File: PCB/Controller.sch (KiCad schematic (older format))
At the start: 1 part

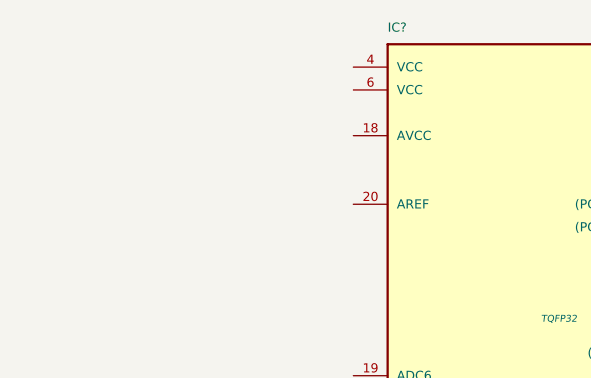
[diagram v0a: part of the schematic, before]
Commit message: Started the schematic. Added the power circuit
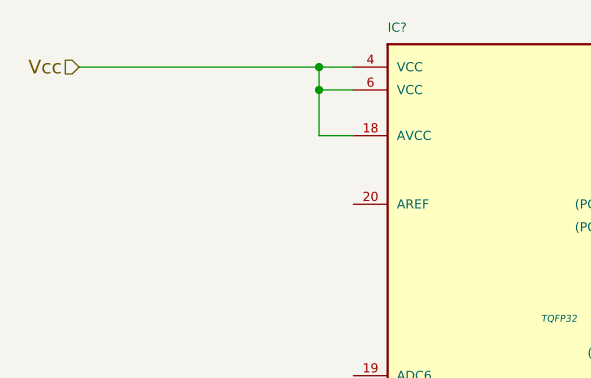
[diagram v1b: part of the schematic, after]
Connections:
- net Vcc: now reaches IC?.18 (AVCC)
- net Vcc: now also IC?.4 (VCC), IC?.6 (VCC)
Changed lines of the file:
@@
 LIBS:memory
 LIBS:xilinx
-LIBS:special
 LIBS:microcontrollers
 LIBS:dsp
@@
 LIBS:contrib
 LIBS:valves
+LIBS:Tfac-Symbols
+LIBS:TfaC-cache
 EELAYER 25 0
 EELAYER END
@@
 	3750 4500 3450 4500
 Connection ~ 3450 4500
+Text HLabel 2550 2200 0    60   Input ~ 0
+Vcc
+Wire Wire Line
+	2550 2200 3750 2200
+Wire Wire Line
+	3600 2200 3600 2500
+Wire Wire Line
+	3600 2300 3750 2300
+Connection ~ 3600 2200
+Wire Wire Line
+	3600 2500 3750 2500
+Connection ~ 3600 2300
 $EndSCHEMATC

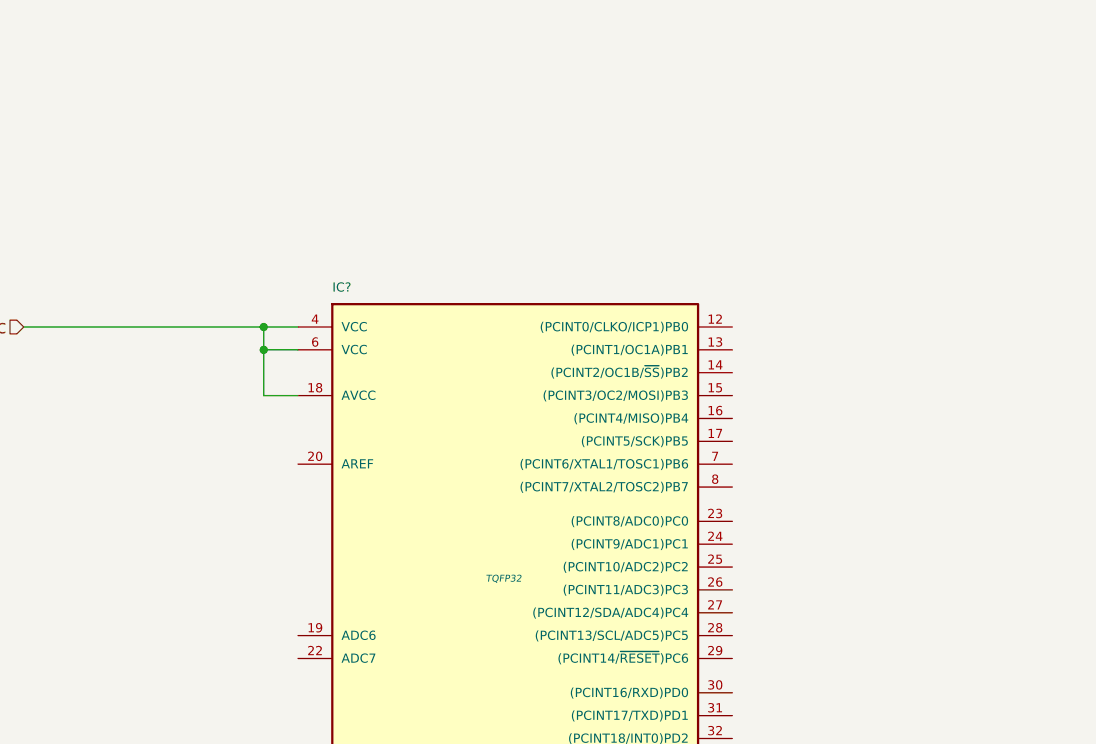
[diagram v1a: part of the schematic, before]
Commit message: Updated the schematic for the RTC and controller
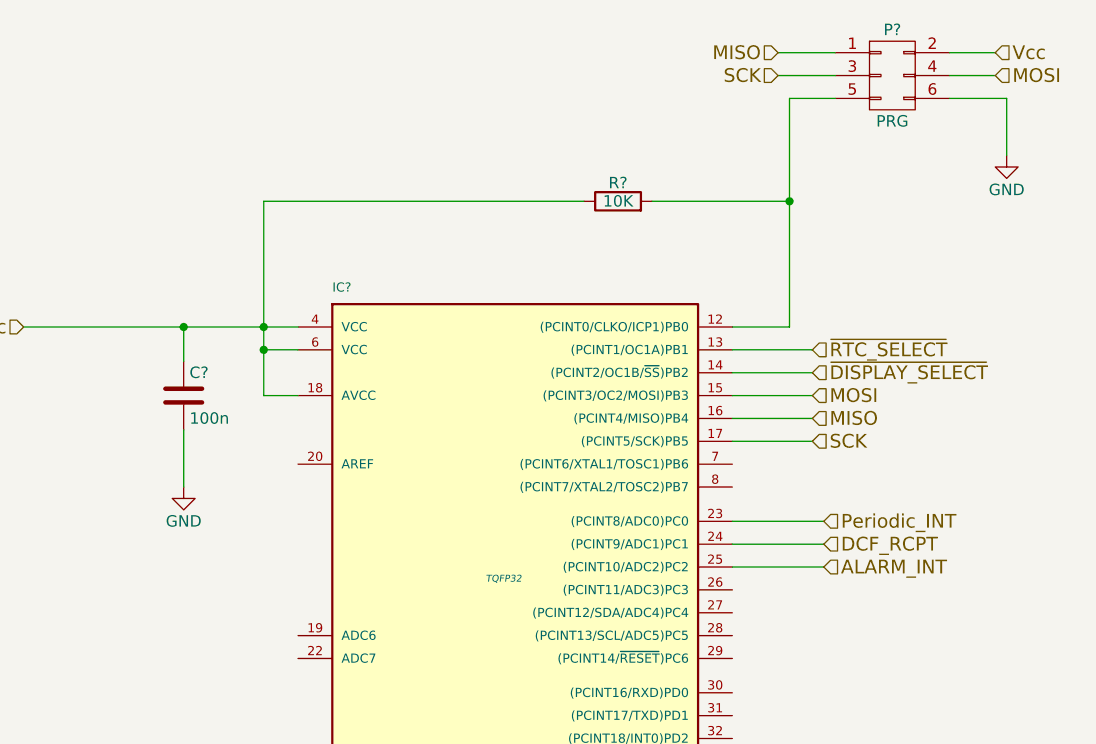
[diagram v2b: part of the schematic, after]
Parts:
- added C?: 100n, symbol C
- added P?: PRG, symbol CONN_02X03
- added R?: 10K, symbol R
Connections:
- net GND: now also C?.2, P?.6 (P6)
- net Vcc: now also C?.1, P?.2 (P2), R?.1
- net at IC?.12 ((PCINT0/CLKO/ICP1)PB0): now also P?.5 (P5), R?.2
- net ~RTC_SELECT: now reaches IC?.13 ((PCINT1/OC1A)PB1)
- net ~DISPLAY_SELECT: now reaches IC?.14 ((PCINT2/OC1B/~SS~)PB2)
- net MOSI: now reaches IC?.15 ((PCINT3/OC2/MOSI)PB3)
- net MOSI: now also P?.4 (P4)
- net MISO: now reaches IC?.16 ((PCINT4/MISO)PB4)
- net MISO: now also P?.1 (P1)
- net SCK: now reaches IC?.17 ((PCINT5/SCK)PB5)
- net SCK: now also P?.3 (P3)
- net Periodic_INT: now reaches IC?.23 ((PCINT8/ADC0)PC0)
- net DCF_RCPT: now reaches IC?.24 ((PCINT9/ADC1)PC1)
- net ALARM_INT: now reaches IC?.25 ((PCINT10/ADC2)PC2)
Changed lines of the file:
@@
 $Descr A4 11693 8268
 encoding utf-8
-Sheet 3 5
+Sheet 5 5
 Title ""
 Date ""
@@
 	2550 2200 3750 2200
 Wire Wire Line
-	3600 2200 3600 2500
+	3600 1650 3600 2500
 Wire Wire Line
 	3600 2300 3750 2300
@@
 	3600 2500 3750 2500
 Connection ~ 3600 2300
+Text HLabel 6000 2500 2    60   Input ~ 0
+MOSI
+Text HLabel 6000 2600 2    60   Input ~ 0
+MISO
+Text HLabel 6000 2700 2    60   Input ~ 0
+SCK
+Text HLabel 6000 2400 2    60   Input ~ 0
+~DISPLAY_SELECT
+Wire Wire Line
+	5650 2400 6000 2400
+Wire Wire Line
+	5650 2500 6000 2500
+Wire Wire Line
+	5650 2600 6000 2600
+Wire Wire Line
+	5650 2700 6000 2700
+Text HLabel 6000 2300 2    60   Input ~ 0
+~RTC_SELECT
+Wire Wire Line
+	5650 2300 6000 2300
+Text HLabel 6050 3050 2    60   Input ~ 0
+Periodic_INT
+Text HLabel 6050 3150 2    60   Input ~ 0
+DCF_RCPT
+Text HLabel 6050 3250 2    60   Input ~ 0
+ALARM_INT
+Wire Wire Line
+	5650 3050 6050 3050
+Wire Wire Line
+	5650 3150 6050 3150
+Wire Wire Line
+	5650 3250 6050 3250
+$Comp
+L CONN_02X03 P?
+U 1 1 5570FD1E
+P 6350 1100
+F 0 "P?" H 6350 1300 50  0000 C CNN
+F 1 "PRG" H 6350 900 50  0000 C CNN
+F 2 "" H 6350 -100 60  0000 C CNN
+F 3 "" H 6350 -100 60  0000 C CNN
+	1    6350 1100
+	1    0    0    -1
+$EndComp
+Text HLabel 5850 1000 0    60   Input ~ 0
+MISO
+Text HLabel 5850 1100 0    60   Input ~ 0
+SCK
+Text HLabel 6800 1100 2    60   Input ~ 0
+MOSI
+Text HLabel 6800 1000 2    60   Input ~ 0
+Vcc
+$Comp
+L GND #PWR?
+U 1 1 5570FE29
+P 6850 1450
+F 0 "#PWR?" H 6850 1200 50  0001 C CNN
+F 1 "GND" H 6850 1300 50  0000 C CNN
+F 2 "" H 6850 1450 60  0000 C CNN
+F 3 "" H 6850 1450 60  0000 C CNN
+	1    6850 1450
+	1    0    0    -1
+$EndComp
+Wire Wire Line
+	6600 1200 6850 1200
+Wire Wire Line
+	6850 1200 6850 1450
+Wire Wire Line
+	6600 1100 6800 1100
+Wire Wire Line
+	6600 1000 6800 1000
+Wire Wire Line
+	6100 1000 5850 1000
+Wire Wire Line
+	6100 1100 5850 1100
+$Comp
+L C C?
+U 1 1 5570FFE4
+P 3250 2500
+F 0 "C?" H 3275 2600 50  0000 L CNN
+F 1 "100n" H 3275 2400 50  0000 L CNN
+F 2 "" H 3288 2350 30  0000 C CNN
+F 3 "" H 3250 2500 60  0000 C CNN
+	1    3250 2500
+	1    0    0    -1
+$EndComp
+Wire Wire Line
+	3250 2350 3250 2200
+Connection ~ 3250 2200
+$Comp
+L GND #PWR?
+U 1 1 55710077
+P 3250 2900
+F 0 "#PWR?" H 3250 2650 50  0001 C CNN
+F 1 "GND" H 3250 2750 50  0000 C CNN
+F 2 "" H 3250 2900 60  0000 C CNN
+F 3 "" H 3250 2900 60  0000 C CNN
+	1    3250 2900
+	1    0    0    -1
+$EndComp
+Wire Wire Line
+	3250 2650 3250 2900
+$Comp
+L R R?
+U 1 1 55710A4C
+P 5150 1650
+F 0 "R?" V 5230 1650 50  0000 C CNN
+F 1 "10K" V 5150 1650 50  0000 C CNN
+F 2 "" V 5080 1650 30  0000 C CNN
+F 3 "" H 5150 1650 30  0000 C CNN
+	1    5150 1650
+	0    -1   -1   0
+$EndComp
+Wire Wire Line
+	5650 2200 5900 2200
+Wire Wire Line
+	5900 2200 5900 1200
+Wire Wire Line
+	5900 1200 6100 1200
+Wire Wire Line
+	5300 1650 5900 1650
+Connection ~ 5900 1650
+Wire Wire Line
+	5000 1650 3600 1650
 $EndSCHEMATC

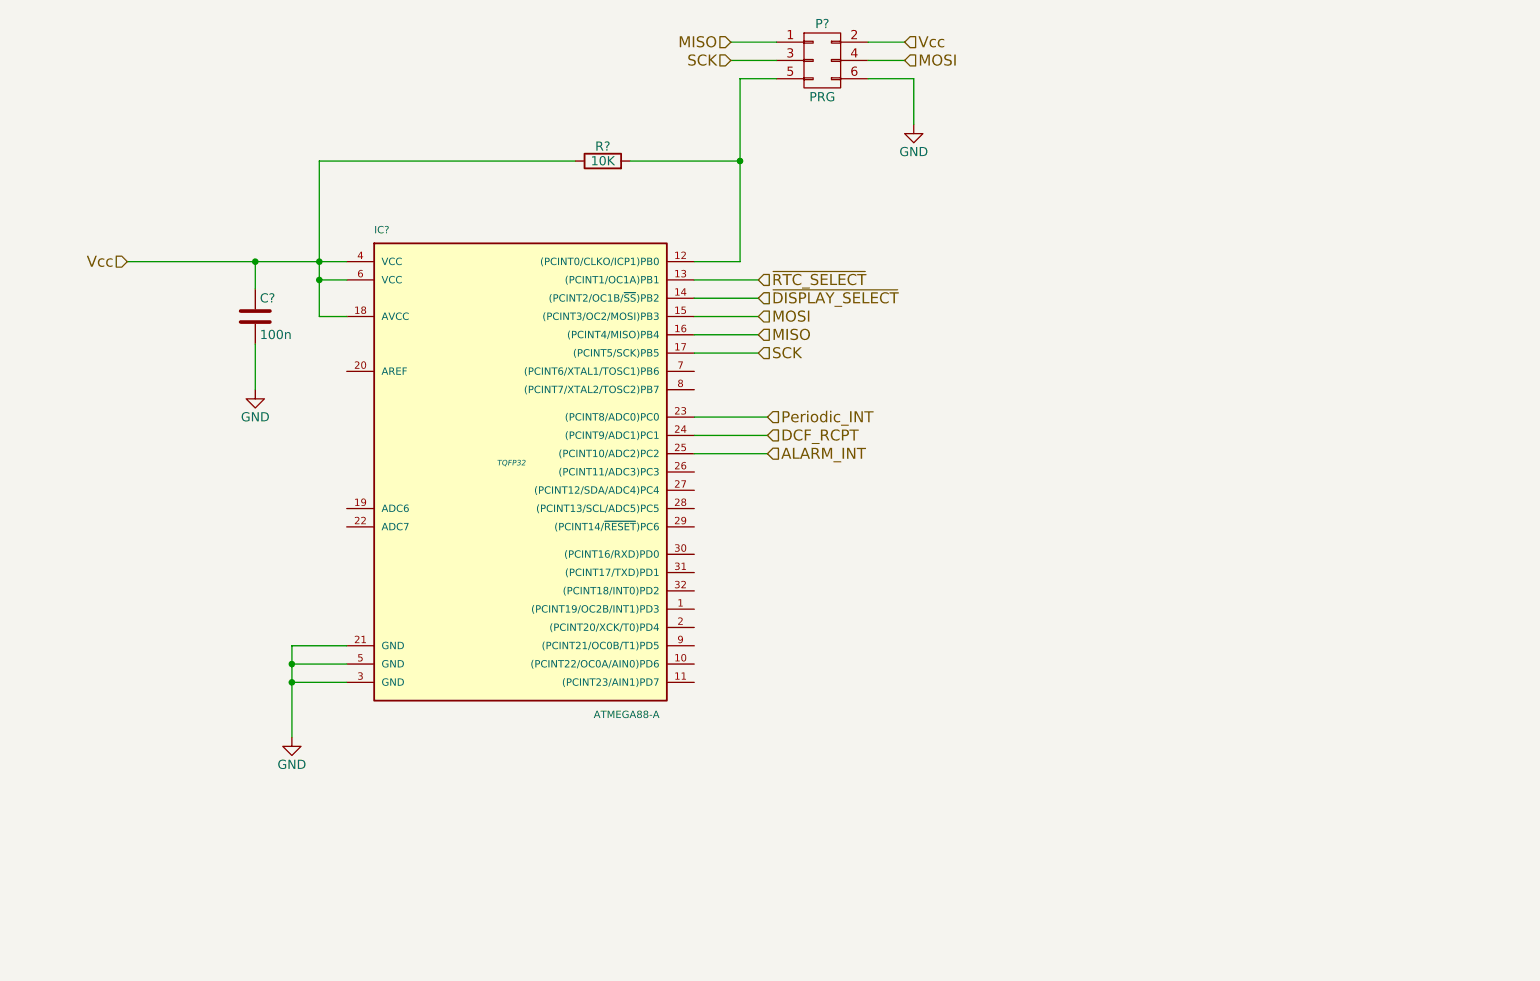
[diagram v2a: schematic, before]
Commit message: correction to the reset circuit
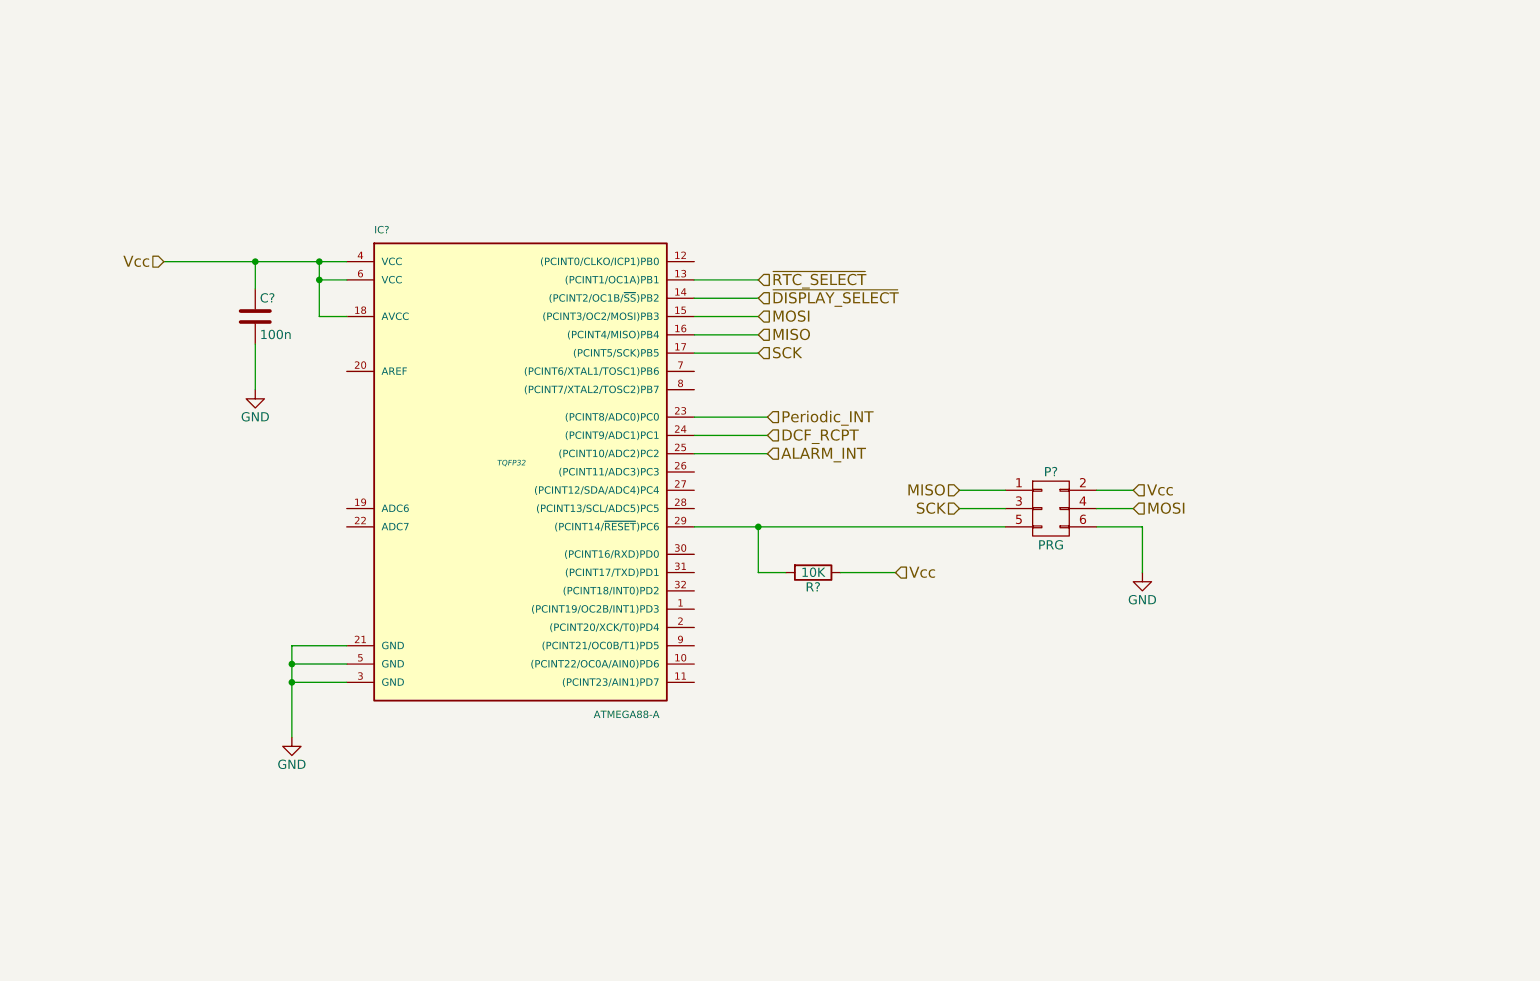
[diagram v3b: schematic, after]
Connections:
- net at P?.5 (P5), R?.2: now also IC?.29 ((PCINT14/~RESET~)PC6); no longer IC?.12 ((PCINT0/CLKO/ICP1)PB0)
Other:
- moved on the sheet: P?, R?
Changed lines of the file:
@@
 LIBS:valves
 LIBS:Tfac-Symbols
-LIBS:TfaC-cache
 EELAYER 25 0
 EELAYER END
@@
 	3750 4500 3450 4500
 Connection ~ 3450 4500
-Text HLabel 2550 2200 0    60   Input ~ 0
+Text HLabel 2750 2200 0    60   Input ~ 0
 Vcc
 Wire Wire Line
-	2550 2200 3750 2200
-Wire Wire Line
-	3600 1650 3600 2500
+	3600 2200 3600 2500
 Wire Wire Line
 	3600 2300 3750 2300
-Connection ~ 3600 2200
 Wire Wire Line
 	3600 2500 3750 2500
@@
 L CONN_02X03 P?
 U 1 1 5570FD1E
-P 6350 1100
-F 0 "P?" H 6350 1300 50  0000 C CNN
-F 1 "PRG" H 6350 900 50  0000 C CNN
-F 2 "" H 6350 -100 60  0000 C CNN
-F 3 "" H 6350 -100 60  0000 C CNN
-	1    6350 1100
+P 7600 3550
+F 0 "P?" H 7600 3750 50  0000 C CNN
+F 1 "PRG" H 7600 3350 50  0000 C CNN
+F 2 "" H 7600 2350 60  0000 C CNN
+F 3 "" H 7600 2350 60  0000 C CNN
+	1    7600 3550
 	1    0    0    -1
 $EndComp
-Text HLabel 5850 1000 0    60   Input ~ 0
+Text HLabel 7100 3450 0    60   Input ~ 0
 MISO
-Text HLabel 5850 1100 0    60   Input ~ 0
+Text HLabel 7100 3550 0    60   Input ~ 0
 SCK
-Text HLabel 6800 1100 2    60   Input ~ 0
+Text HLabel 8050 3550 2    60   Input ~ 0
 MOSI
-Text HLabel 6800 1000 2    60   Input ~ 0
+Text HLabel 8050 3450 2    60   Input ~ 0
 Vcc
 $Comp
 L GND #PWR?
 U 1 1 5570FE29
-P 6850 1450
-F 0 "#PWR?" H 6850 1200 50  0001 C CNN
-F 1 "GND" H 6850 1300 50  0000 C CNN
-F 2 "" H 6850 1450 60  0000 C CNN
-F 3 "" H 6850 1450 60  0000 C CNN
-	1    6850 1450
+P 8100 3900
+F 0 "#PWR?" H 8100 3650 50  0001 C CNN
+F 1 "GND" H 8100 3750 50  0000 C CNN
+F 2 "" H 8100 3900 60  0000 C CNN
+F 3 "" H 8100 3900 60  0000 C CNN
+	1    8100 3900
 	1    0    0    -1
 $EndComp
 Wire Wire Line
-	6600 1200 6850 1200
+	7850 3650 8100 3650
 Wire Wire Line
-	6850 1200 6850 1450
+	8100 3650 8100 3900
 Wire Wire Line
-	6600 1100 6800 1100
+	7850 3550 8050 3550
 Wire Wire Line
-	6600 1000 6800 1000
+	7850 3450 8050 3450
 Wire Wire Line
-	6100 1000 5850 1000
+	7350 3450 7100 3450
 Wire Wire Line
-	6100 1100 5850 1100
+	7350 3550 7100 3550
 $Comp
 L C C?
@@
 	1    0    0    -1
 $EndComp
-Wire Wire Line
-	3250 2350 3250 2200
-Connection ~ 3250 2200
 $Comp
 L GND #PWR?
@@
 L R R?
 U 1 1 55710A4C
-P 5150 1650
-F 0 "R?" V 5230 1650 50  0000 C CNN
-F 1 "10K" V 5150 1650 50  0000 C CNN
-F 2 "" V 5080 1650 30  0000 C CNN
-F 3 "" H 5150 1650 30  0000 C CNN
-	1    5150 1650
-	0    -1   -1   0
+P 6300 3900
+F 0 "R?" V 6380 3900 50  0000 C CNN
+F 1 "10K" V 6300 3900 50  0000 C CNN
+F 2 "" V 6230 3900 30  0000 C CNN
+F 3 "" H 6300 3900 30  0000 C CNN
+	1    6300 3900
+	0    1    1    0
 $EndComp
 Wire Wire Line
-	5650 2200 5900 2200
+	5650 3650 7350 3650
 Wire Wire Line
-	5900 2200 5900 1200
+	2750 2200 3750 2200
+Connection ~ 3600 2200
+Text HLabel 6750 3900 2    60   Input ~ 0
+Vcc
 Wire Wire Line
-	5900 1200 6100 1200
+	6750 3900 6450 3900
 Wire Wire Line
-	5300 1650 5900 1650
-Connection ~ 5900 1650
+	6150 3900 6000 3900
 Wire Wire Line
-	5000 1650 3600 1650
+	6000 3900 6000 3650
+Connection ~ 6000 3650
+Wire Wire Line
+	3250 2350 3250 2200
+Connection ~ 3250 2200
 $EndSCHEMATC

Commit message: Generated the Netlist and started associating footprints
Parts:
- added SW501: Time Set, symbol SW_PUSH
- added SW502: Alarm Set, symbol SW_PUSH
- added SW503: Fast, symbol SW_PUSH
- added SW504: Slow, symbol SW_PUSH
- added SW505: Auto Time, symbol SW_PUSH
- added SW506, SW507: Sleep, symbol SW_PUSH
- added SW508: Alarm Enabled, symbol SPST
- C501: renamed from C?; footprint (none) -> Capacitors_SMD:C_0805_HandSoldering
- IC501: renamed from IC?; footprint TQFP32 -> Housings_QFP:LQFP-32_7x7mm_Pitch0.8mm
- P501: renamed from P?; footprint (none) -> Pin_Headers:Pin_Header_Straight_2x03
- R501: renamed from R?; footprint (none) -> Resistors_SMD:R_0805_HandSoldering
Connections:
- net labels added: Alarm_Enabled, Alarm_Set, Auto_Time, Fast, Reset, Sleep, Slow, Summer_Time, Time_Set
- wire segments 28 -> 54
- no-connect marks 0 -> 9
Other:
- moved on the sheet: C501, P501, R501
